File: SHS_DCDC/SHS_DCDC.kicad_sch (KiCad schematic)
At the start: 24 parts, among them J1 Barrel_Jack, Q1 BSS84, Q14 2N7002, Q15 MOSP_GENERIC, Q16 MOSP_GENERIC, U1 RT8299-WDFN10L

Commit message: Ubuntu transfer
Commit before transfer onto Ubuntu
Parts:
- removed Q14: 2N7002, Package_TO_SOT_SMD:SOT-23, symbol Transistor_FET:2N7002
- removed Q15, Q16: MOSP_GENERIC, Package_TO_SOT_SMD:SOT-23, symbol SHS_DCDC:MOSP_GENERIC
- removed R46: 1k, Resistor_SMD:R_0603_1608Metric, symbol SHS_DCDC:R-Device
- removed R47: 100k, Resistor_SMD:R_0402_1005Metric, symbol SHS_DCDC:R-Device
- added C35: 100nF, Capacitor_SMD:C_0402_1005Metric, symbol SHS_DCDC:C-Device
- added Q14, Q16: PMV100XPEAR, digikey-kicad-library-master:SOT-23-3, symbol SHS_DCDC:PMV100XPEAR
- added Q15: BSS84, Package_TO_SOT_SMD:SOT-23, symbol SHS_DCDC:BSS84-Transistor_FET
- R1: value R -> 100k
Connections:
- net DCDC_OUT: now also Q16.3 (D)
- net GND: now also C35.1, Q15.3 (D)
- net MCU_MPPT_ENABLE: now also R48.1, U1.3 (EN), C35.2, Q15.1 (G)
- net at C30.1, C31.1, J1.1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: now also R1.1, Q14.3 (D)
- net MCU_PVBAT_DIRECT: no longer names the net of R1.2
- net MCU_PVBAT_DIRECT: now also Q14.1 (G), Q15.2 (S), Q16.1 (G)
- new net: Q14.2 (S), Q16.2 (S)
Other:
- moved on the sheet: C1, C2, C30, C31, C32, C4, C5, J1, L1, R3, R48, U1

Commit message: Commit_Fix
Fix to move back to ESP32
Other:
- note added: "Bidirectional switch"
- note added: "MCU_MPPT_ENABLE working principles: Sig 0 --> MPPT disabled, DCDC conv disabled, PV power flow through the bidirectional switch Sig 1 --> MPPT activated, DCDC conv enabled, bidirectional switch disabled, PV power flow through DCDC Sig is driven by the MCU. The MCU drives Sig if it is powered, otherwise Sig = 0 (pull down) Sig is activated by MCU when the Vbat is high enough (user setting)"
- moved on the sheet: C1, C2, C30, C31, C32, C33, C34, C35, C4, C5, J1, L1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

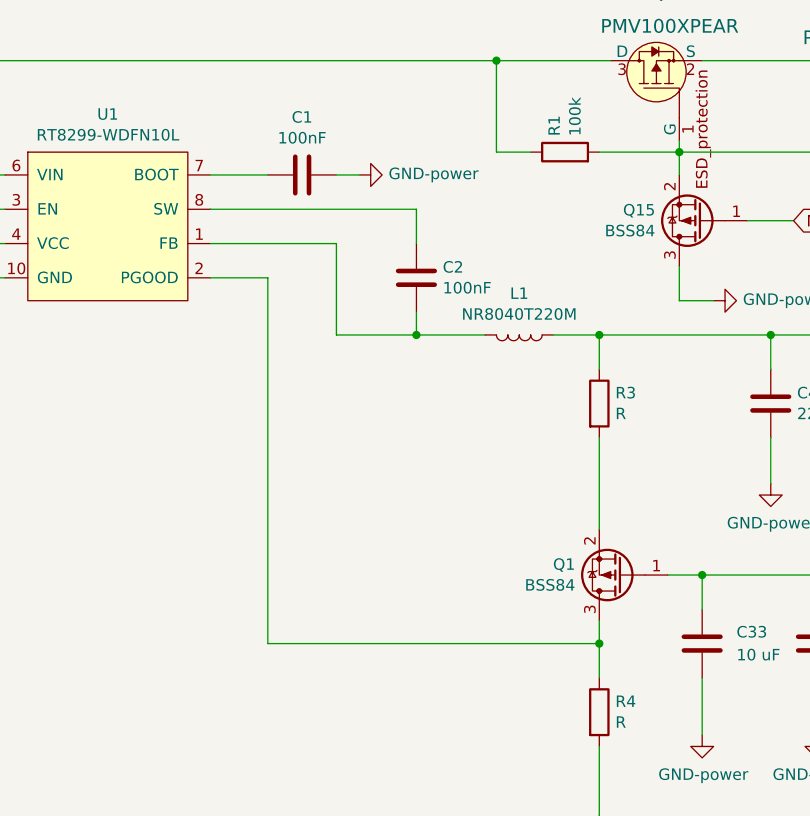
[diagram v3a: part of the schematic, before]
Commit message: Error fix on DCDC block
Wrong pinout on DCDC block that needed to be fixed
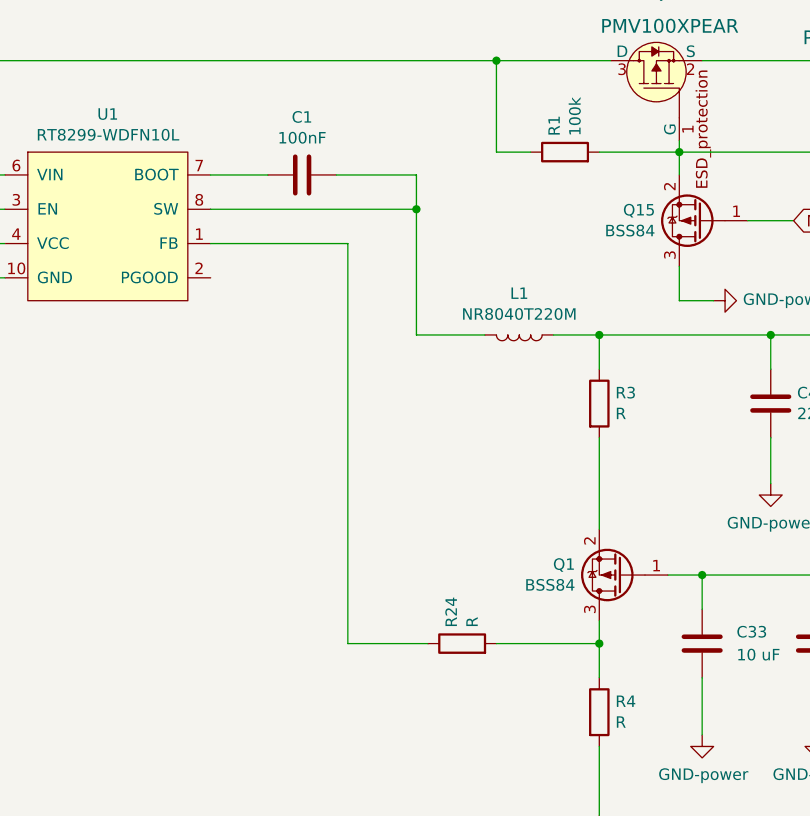
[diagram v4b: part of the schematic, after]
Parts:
- removed C2: 100nF, Capacitor_SMD:C_0603_1608Metric, symbol SHS_DCDC:C-Device
- added R24: R, Resistor_SMD:R_0603_1608Metric, symbol SHS_DCDC:R-Device
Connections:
- net GND: no longer C1.2
- net at U1.8 (SW): now also C1.2, L1.2
- net at U1.1 (FB): now also R24.1; no longer L1.2
- net at Q1.3 (D), R4.1: now also R24.2; no longer U1.2 (PGOOD)
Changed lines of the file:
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@@
   (junction (at 100.33 62.23) (diameter 0) (color 0 0 0 0)
   )
-  (junction (at 179.07 76.2) (diameter 0) (color 0 0 0 0)
-  )
   (junction (at 208.28 55.88) (diameter 0) (color 0 0 0 0)
   )
+  (junction (at 179.07 62.23) (diameter 0) (color 0 0 0 0)
+  )
   (junction (at 199.39 76.2) (diameter 0) (color 0 0 0 0)
   )
@@
     (stroke (width 0) (type default) (color 0 0 0 0))
   )
-  (wire (pts (xy 179.07 76.2) (xy 179.07 73.66))
-    (stroke (width 0) (type default) (color 0 0 0 0))
-  )
   (wire (pts (xy 90.17 62.23) (xy 93.98 62.23))
     (stroke (width 0) (type default) (color 0 0 0 0))
@@
     (stroke (width 0) (type default) (color 0 0 0 0))
   )
-  (wire (pts (xy 179.07 62.23) (xy 179.07 66.04))
-    (stroke (width 0) (type default) (color 0 0 0 0))
-  )
   (wire (pts (xy 208.28 68.58) (xy 208.28 72.39))
     (stroke (width 0) (type default) (color 0 0 0 0))
   )
-  (wire (pts (xy 162.56 110.49) (xy 199.39 110.49))
+  (wire (pts (xy 171.45 110.49) (xy 180.34 110.49))
     (stroke (width 0) (type default) (color 0 0 0 0))
   )
@@
     (stroke (width 0) (type default) (color 0 0 0 0))
   )
-  (wire (pts (xy 170.18 76.2) (xy 179.07 76.2))
+  (wire (pts (xy 179.07 76.2) (xy 186.69 76.2))
     (stroke (width 0) (type default) (color 0 0 0 0))
   )
@@
     (stroke (width 0) (type default) (color 0 0 0 0))
   )
+  (wire (pts (xy 187.96 110.49) (xy 199.39 110.49))
+    (stroke (width 0) (type default) (color 0 0 0 0))
+  )
   (wire (pts (xy 100.33 62.23) (xy 100.33 68.58))
     (stroke (width 0) (type default) (color 0 0 0 0))
@@
     (stroke (width 0) (type default) (color 0 0 0 0))
   )
+  (wire (pts (xy 156.21 66.04) (xy 171.45 66.04))
+    (stroke (width 0) (type default) (color 0 0 0 0))
+  )
   (wire (pts (xy 93.98 62.23) (xy 100.33 62.23))
     (stroke (width 0) (type default) (color 0 0 0 0))
@@
     (stroke (width 0) (type default) (color 0 0 0 0))
   )
-  (wire (pts (xy 156.21 66.04) (xy 170.18 66.04))
-    (stroke (width 0) (type default) (color 0 0 0 0))
-  )
   (wire (pts (xy 246.38 114.3) (xy 246.38 119.38))
     (stroke (width 0) (type default) (color 0 0 0 0))
@@
     (stroke (width 0) (type default) (color 0 0 0 0))
   )
-  (wire (pts (xy 162.56 69.85) (xy 162.56 110.49))
-    (stroke (width 0) (type default) (color 0 0 0 0))
-  )
-  (wire (pts (xy 170.18 66.04) (xy 170.18 76.2))
+  (wire (pts (xy 171.45 66.04) (xy 171.45 110.49))
+    (stroke (width 0) (type default) (color 0 0 0 0))
+  )
+  (wire (pts (xy 179.07 62.23) (xy 179.07 76.2))
     (stroke (width 0) (type default) (color 0 0 0 0))
   )
@@
     (stroke (width 0) (type default) (color 0 0 0 0))
   )
-  (wire (pts (xy 156.21 69.85) (xy 162.56 69.85))
-    (stroke (width 0) (type default) (color 0 0 0 0))
-  )
   (wire (pts (xy 215.9 63.5) (xy 220.98 63.5))
     (stroke (width 0) (type default) (color 0 0 0 0))
@@
     (stroke (width 0) (type default) (color 0 0 0 0))
   )
-  (wire (pts (xy 172.72 58.42) (xy 170.18 58.42))
+  (wire (pts (xy 170.18 58.42) (xy 179.07 58.42))
     (stroke (width 0) (type default) (color 0 0 0 0))
   )
@@
     (stroke (width 0) (type default) (color 0 0 0 0))
   )
+  (wire (pts (xy 179.07 58.42) (xy 179.07 62.23))
+    (stroke (width 0) (type default) (color 0 0 0 0))
+  )
   (wire (pts (xy 247.65 45.72) (xy 247.65 76.2))
     (stroke (width 0) (type default) (color 0 0 0 0))
@@
   )
   (wire (pts (xy 113.03 66.04) (xy 133.35 66.04))
-    (stroke (width 0) (type default) (color 0 0 0 0))
-  )
-  (wire (pts (xy 179.07 76.2) (xy 186.69 76.2))
     (stroke (width 0) (type default) (color 0 0 0 0))
   )
@@
     )
     (property "Datasheet" "~" (id 3) (at 166.37 58.42 0)
-      (effects (font (size 1.27 1.27)) hide)
-    )
-    (pin "1")
-    (pin "2")
-  )
-  (symbol (lib_id "SHS_DCDC:GND-power") (at 172.72 58.42 90) (unit 1)
-    (in_bom yes) (on_board yes)
-    (property "Reference" "#PWR0102" (id 0) (at 179.07 58.42 0)
-      (effects (font (size 1.27 1.27)) hide)
-    )
-    (property "Value" "GND-power" (id 1) (at 175.9712 58.293 90)
-      (effects (font (size 1.27 1.27)) (justify right))
-    )
-    (property "Footprint" "" (id 2) (at 172.72 58.42 0)
-      (effects (font (size 1.27 1.27)) hide)
-    )
-    (property "Datasheet" "" (id 3) (at 172.72 58.42 0)
-      (effects (font (size 1.27 1.27)) hide)
-    )
-    (pin "1")
-  )
-  (symbol (lib_id "SHS_DCDC:C-Device") (at 179.07 69.85 0) (unit 1)
-    (in_bom yes) (on_board yes)
-    (property "Reference" "C2" (id 0) (at 181.991 68.6816 0)
-      (effects (font (size 1.27 1.27)) (justify left))
-    )
-    (property "Value" "100nF" (id 1) (at 181.991 70.993 0)
-      (effects (font (size 1.27 1.27)) (justify left))
-    )
-    (property "Footprint" "Capacitor_SMD:C_0603_1608Metric" (id 2) (at 180.0352 73.66 0)
-      (effects (font (size 1.27 1.27)) hide)
-    )
-    (property "Datasheet" "~" (id 3) (at 179.07 69.85 0)
       (effects (font (size 1.27 1.27)) hide)
     )
@@
     )
     (pin "1")
+  )
+  (symbol (lib_id "SHS_DCDC:R-Device") (at 184.15 110.49 90) (unit 1)
+    (in_bom yes) (on_board yes)
+    (property "Reference" "R24" (id 0) (at 182.9816 108.712 0)
+      (effects (font (size 1.27 1.27)) (justify left))
+    )
+    (property "Value" "R" (id 1) (at 185.293 108.712 0)
+      (effects (font (size 1.27 1.27)) (justify left))
+    )
+    (property "Footprint" "Resistor_SMD:R_0603_1608Metric" (id 2) (at 184.15 112.268 90)
+      (effects (font (size 1.27 1.27)) hide)
+    )
+    (property "Datasheet" "~" (id 3) (at 184.15 110.49 0)
+      (effects (font (size 1.27 1.27)) hide)
+    )
+    (pin "1")
+    (pin "2")
   )
   (symbol (lib_id "Device:C") (at 223.52 110.49 0) (unit 1)
@@
       (reference "#PWR0101") (unit 1) (value "GND-power") (footprint "")
     )
-    (path "/00000000-0000-0000-0000-0000603dc622"
-      (reference "#PWR0102") (unit 1) (value "GND-power") (footprint "")
-    )
     (path "/a76ffc62-1853-46d7-a1b3-01061ef89817/4e45e128-10f5-41be-8c95-96bdcfe6a530"
       (reference "#PWR0103") (unit 1) (value "GND-power") (footprint "")
@@
       (reference "C1") (unit 1) (value "100nF") (footprint "Capacitor_SMD:C_0402_1005Metric")
     )
-    (path "/00000000-0000-0000-0000-0000603ec5c6"
-      (reference "C2") (unit 1) (value "100nF") (footprint "Capacitor_SMD:C_0603_1608Metric")
-    )
     (path "/a76ffc62-1853-46d7-a1b3-01061ef89817/52b681f4-c0d3-4ad3-813b-da0560698d1f"
       (reference "C3") (unit 1) (value "100nF") (footprint "Capacitor_SMD:C_0603_1608Metric")
@@
       (reference "R23") (unit 1) (value "100k") (footprint "Resistor_SMD:R_0603_1608Metric")
     )
+    (path "/3f23ceda-b583-4224-9e30-e02c60d78220"
+      (reference "R24") (unit 1) (value "R") (footprint "Resistor_SMD:R_0603_1608Metric")
+    )
     (path "/00000000-0000-0000-0000-0000605796bf/00000000-0000-0000-0000-0000607bfe33"

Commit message: ProgressMisc
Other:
- moved on the sheet: R3
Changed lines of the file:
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@@
     (stroke (width 0) (type default) (color 0 0 0 0))
   )
-  (wire (pts (xy 199.39 87.63) (xy 199.39 97.79))
+  (wire (pts (xy 199.39 91.44) (xy 199.39 97.79))
     (stroke (width 0) (type default) (color 0 0 0 0))
   )
@@
     (stroke (width 0) (type default) (color 0 0 0 0))
   )
-  (wire (pts (xy 199.39 80.01) (xy 199.39 76.2))
+  (wire (pts (xy 199.39 83.82) (xy 199.39 76.2))
     (stroke (width 0) (type default) (color 0 0 0 0))
   )
@@
     (pin "2")
   )
-  (symbol (lib_id "SHS_DCDC:R-Device") (at 199.39 83.82 0) (unit 1)
-    (in_bom yes) (on_board yes)
-    (property "Reference" "R3" (id 0) (at 201.168 82.6516 0)
-      (effects (font (size 1.27 1.27)) (justify left))
-    )
-    (property "Value" "R" (id 1) (at 201.168 84.963 0)
-      (effects (font (size 1.27 1.27)) (justify left))
-    )
-    (property "Footprint" "Resistor_SMD:R_0603_1608Metric" (id 2) (at 197.612 83.82 90)
-      (effects (font (size 1.27 1.27)) hide)
-    )
-    (property "Datasheet" "~" (id 3) (at 199.39 83.82 0)
+  (symbol (lib_id "SHS_DCDC:R-Device") (at 199.39 87.63 0) (unit 1)
+    (in_bom yes) (on_board yes)
+    (property "Reference" "R3" (id 0) (at 201.168 86.4616 0)
+      (effects (font (size 1.27 1.27)) (justify left))
+    )
+    (property "Value" "R" (id 1) (at 201.168 88.773 0)
+      (effects (font (size 1.27 1.27)) (justify left))
+    )
+    (property "Footprint" "Resistor_SMD:R_0603_1608Metric" (id 2) (at 197.612 87.63 90)
+      (effects (font (size 1.27 1.27)) hide)
+    )
+    (property "Datasheet" "~" (id 3) (at 199.39 87.63 0)
       (effects (font (size 1.27 1.27)) hide)
     )
@@
       (reference "#PWR0101") (unit 1) (value "GND-power") (footprint "")
     )
+    (path "/00000000-0000-0000-0000-000060624557/3b0a89a9-e0e8-45ff-b2ce-52f998a72ced"
+      (reference "#PWR0102") (unit 1) (value "GND-power") (footprint "")
+    )
     (path "/a76ffc62-1853-46d7-a1b3-01061ef89817/4e45e128-10f5-41be-8c95-96bdcfe6a530"
       (reference "#PWR0103") (unit 1) (value "GND-power") (footprint "")
@@
       (reference "#PWR0122") (unit 1) (value "GND-power") (footprint "")
     )
+    (path "/00000000-0000-0000-0000-000060624557/3d5f5369-f3ac-4ea1-9650-b2d55c053b83"
+      (reference "#PWR0123") (unit 1) (value "GND-power") (footprint "")
+    )
     (path "/00000000-0000-0000-0000-0000604584af/00000000-0000-0000-0000-000060cbd25b"
       (reference "4cells1") (unit 1) (value "BK-18650-PC8") (footprint "BK-18650:BK-18650-PC8")
@@
       (reference "C1") (unit 1) (value "100nF") (footprint "Capacitor_SMD:C_0402_1005Metric")
     )
+    (path "/00000000-0000-0000-0000-000060624557/a32bb310-073c-427c-bc59-f751ee5d5479"
+      (reference "C2") (unit 1) (value "TBD") (footprint "Capacitor_SMD:C_0402_1005Metric")
+    )
     (path "/a76ffc62-1853-46d7-a1b3-01061ef89817/52b681f4-c0d3-4ad3-813b-da0560698d1f"
       (reference "C3") (unit 1) (value "100nF") (footprint "Capacitor_SMD:C_0603_1608Metric")
@@
       (reference "C36") (unit 1) (value "1uF") (footprint "Capacitor_SMD:C_0402_1005Metric")
     )
+    (path "/00000000-0000-0000-0000-000060624557/380d7429-6590-487a-bba3-b7ca092c57f1"
+      (reference "C37") (unit 1) (value "TBD") (footprint "Capacitor_SMD:C_0402_1005Metric")
+    )
     (path "/00000000-0000-0000-0000-0000604ea25d"
       (reference "J1") (unit 1) (value "Barrel_Jack") (footprint "digikey-footprints:Barrel_Jack_5.5mmODx2.1mmID_PJ-202A")
@@
       (reference "U7") (unit 1) (value "MCP101") (footprint "Package_TO_SOT_SMD:SOT-23")
     )
-  )
+    (path "/00000000-0000-0000-0000-000060624557/db6a7003-3691-4714-9ddf-9f98274a9c8c"
+      (reference "Y1") (unit 1) (value "2-SMD no lead") (footprint "Crystal:Crystal_SMD_3215-2Pin_3.2x1.5mm")
+    )
+  )

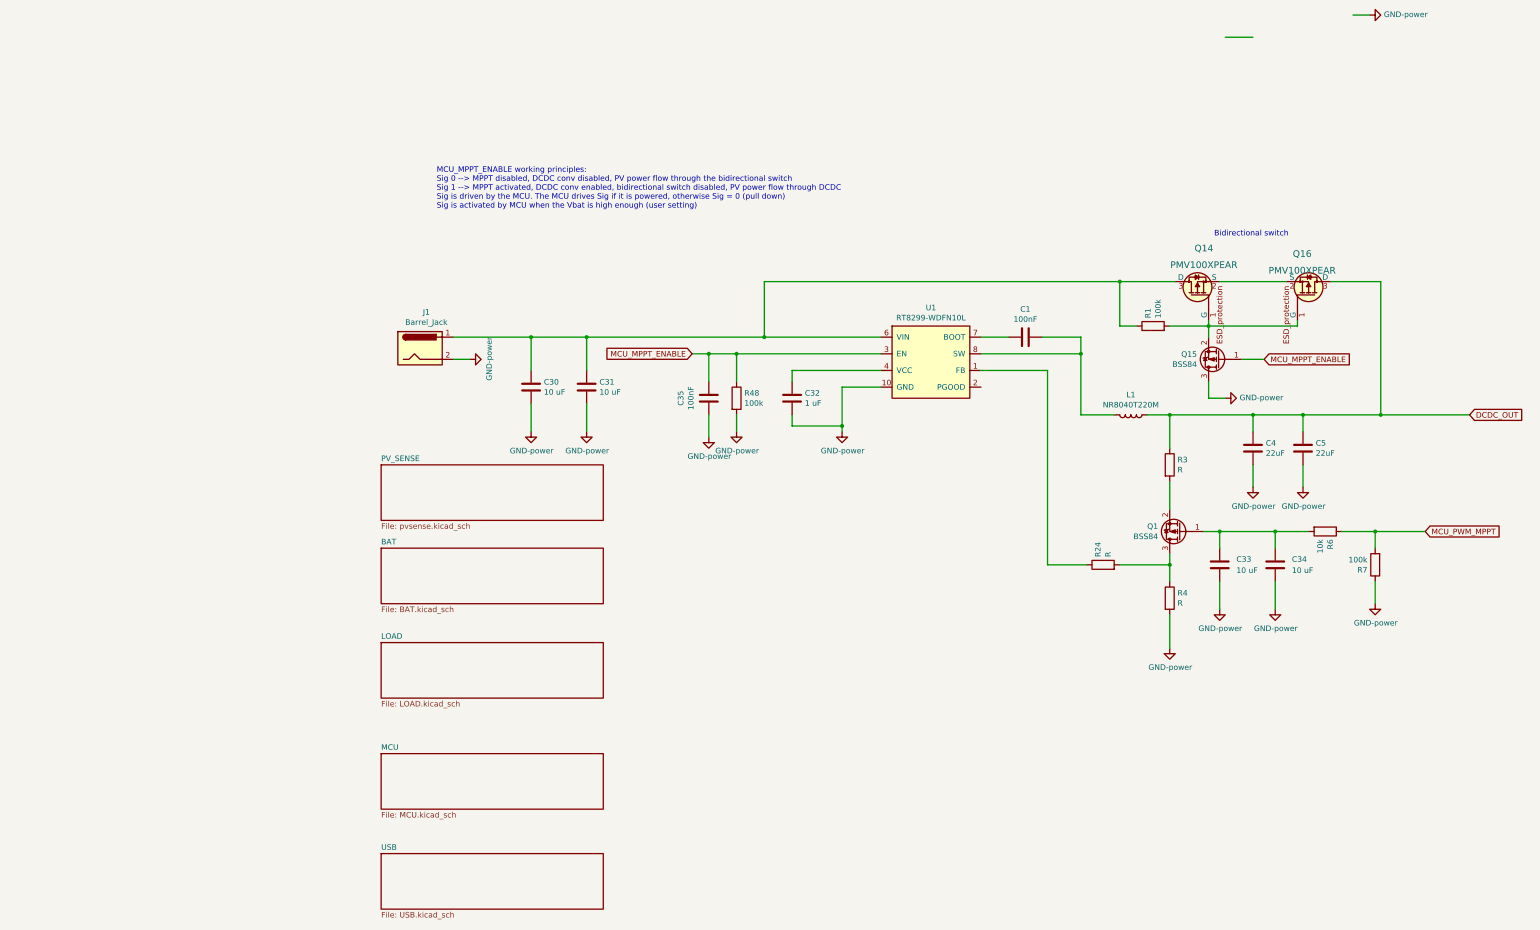
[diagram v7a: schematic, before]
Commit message: PV & BAT V sense
Adding 2 same blocks allowing the measure by ADC of the PV and Battery voltage on demand through power gating technique
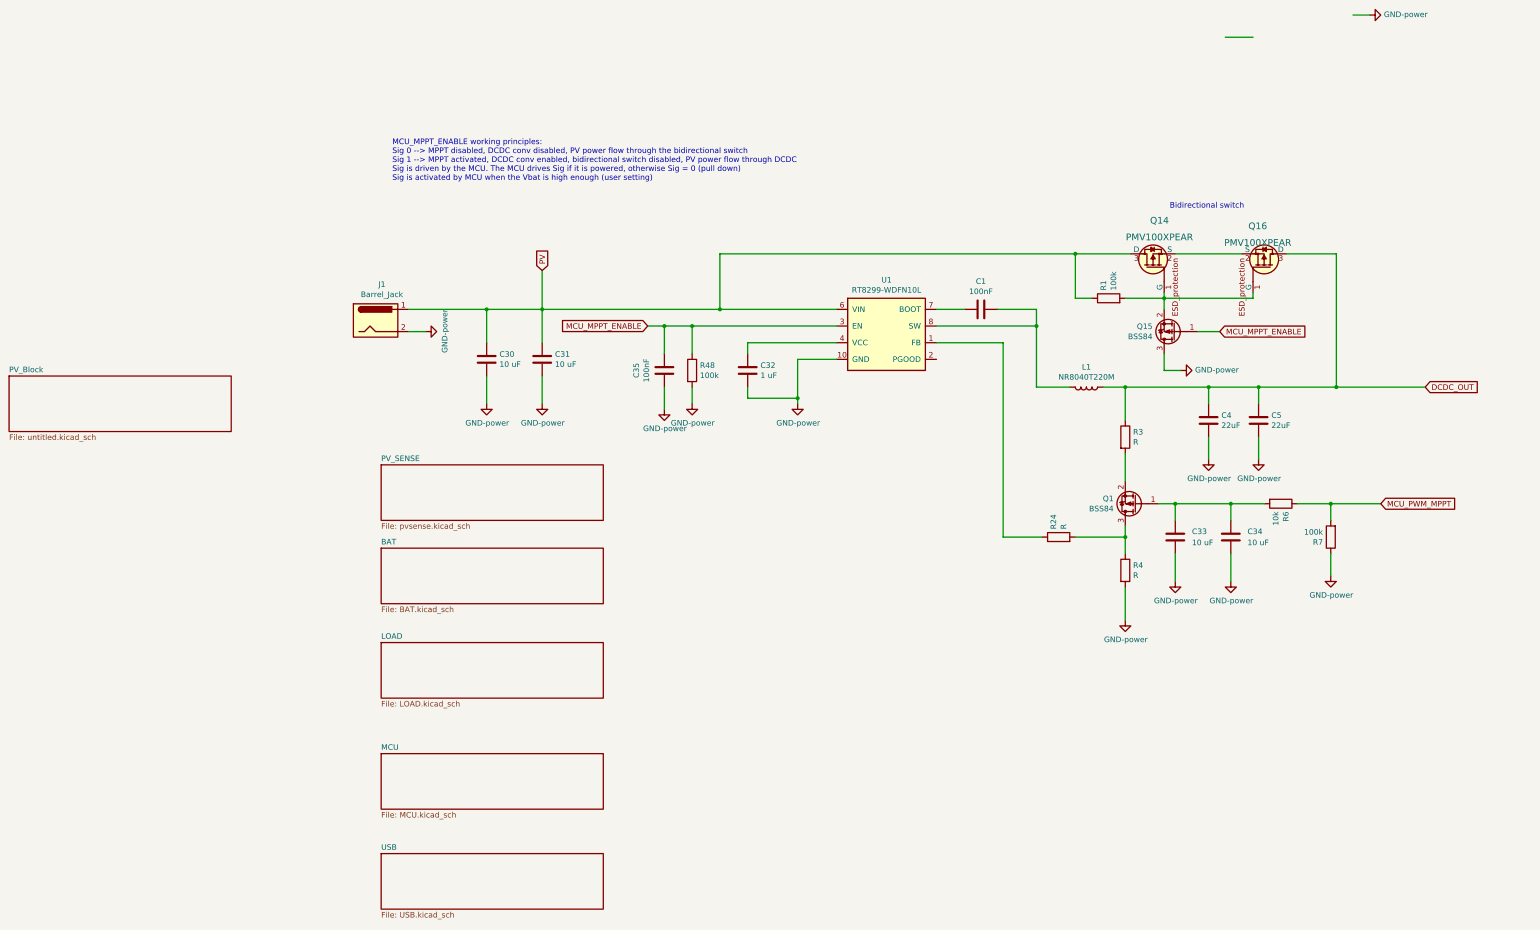
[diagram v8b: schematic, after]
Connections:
- net PV: now reaches C30.1, C31.1, J1.1, Q14.3 (D), R1.1, U1.6 (VIN)
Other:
- added sheet PV_Block (untitled.kicad_sch)
- moved on the sheet: C1, C30, C31, C32, C33, C34, C35, C4, C5, J1, L1, Q1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
